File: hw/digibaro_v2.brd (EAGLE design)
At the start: 109 x 78.5 mm, 11 parts

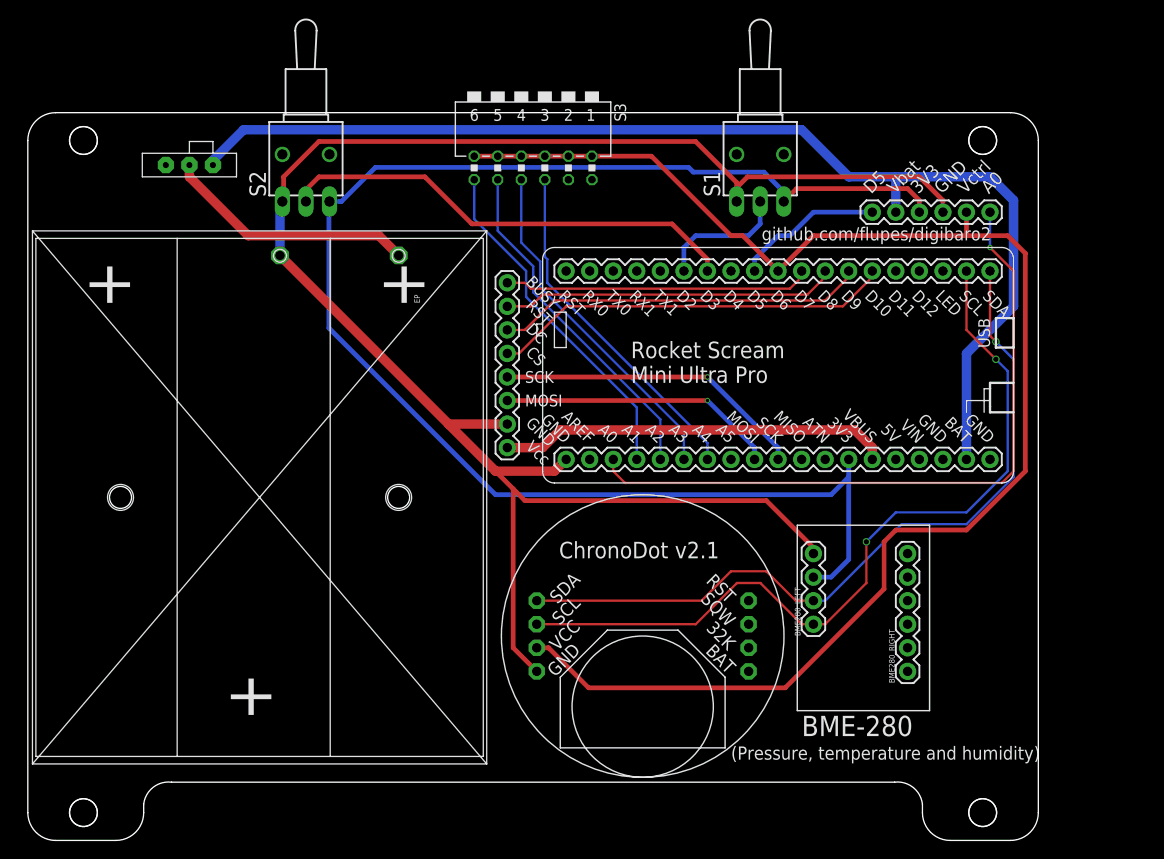
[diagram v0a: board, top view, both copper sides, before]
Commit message: fixed schematic, corrected footprint (switch + rocket scream) and improved layout
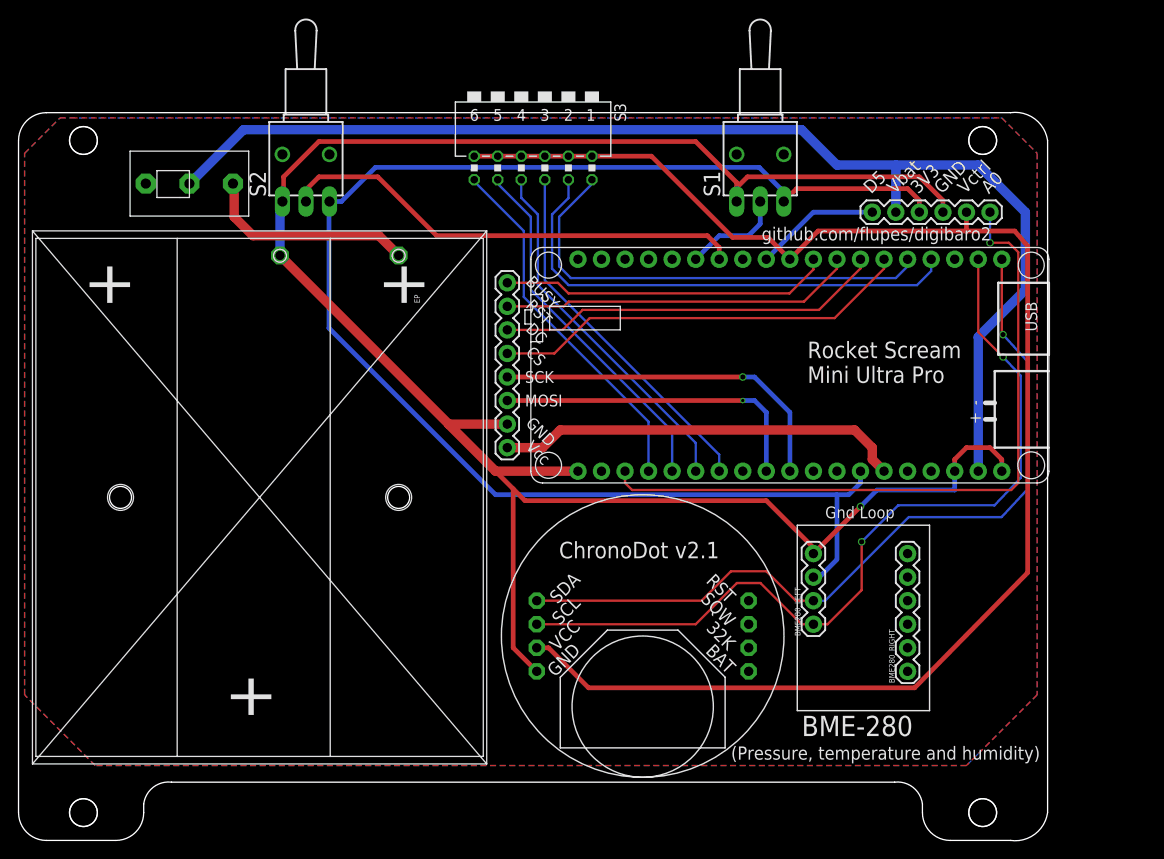
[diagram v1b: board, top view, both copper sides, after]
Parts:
- U$2: value SLIDE-SWITCHSS12SDH2 -> SLIDE-SWITCHNKKMINIATURE; device flupes:SS12SDH2 -> flupes:MS12ANG03
- moved U$2 2.00 mm to (11.4, 67.8)
- moved U$3 1.27 mm to (76.2, 48.3)
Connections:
- removed net MISO: U$3.MISO
- removed net N$14: U$2.P$3
- removed net N$5: U$3.A5
- net GND: now also U$3.GND2, U$3.GND3
- net TZ1: now also U$3.D11
- net TZ2: now also U$3.D12
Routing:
- net TZ2: track 0.00 -> 53.9 mm
- net TZ1: track 0.00 -> 50.2 mm
- net GND: track 196.0 -> 225.5 mm, vias 0 -> 1
- net VBAT: track 125.2 -> 131.4 mm
- net SCK: track 33.6 -> 38.4 mm
- net MOSI: track 30.0 -> 34.8 mm
- net POS: track 27.4 -> 23.1 mm
- net SDA: track 82.9 -> 86.5 mm
- net SCL: track 87.4 -> 91.0 mm
- net VCTRL: track 160.1 -> 163.5 mm
- net N$6: track 14.2 -> 11.0 mm
- net 3V3: track 163.0 -> 160.2 mm
- net D5: track 16.1 -> 13.5 mm
- net BUSY: track 33.2 -> 35.7 mm
- net EPRST: track 36.2 -> 38.3 mm
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- added copper zone on layer 1, net GND
- added copper zone on layer 16, net GND
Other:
- board size 109 x 78.5 mm -> 111 x 78.6 mm
- board text added: "Gnd Loop"
